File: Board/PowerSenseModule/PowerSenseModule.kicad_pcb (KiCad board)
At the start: 2 copper layers, 54 parts, among them J1 Power IO, J2 CAN IO, J3 Programming Header, U1 TPS82150, U2 ZLDO117, U3 dsPIC33EP32GP502_QFN, U4 MCP2542FDxMF, U5 MCP9700AT-ETT, U6 MCP39F511A

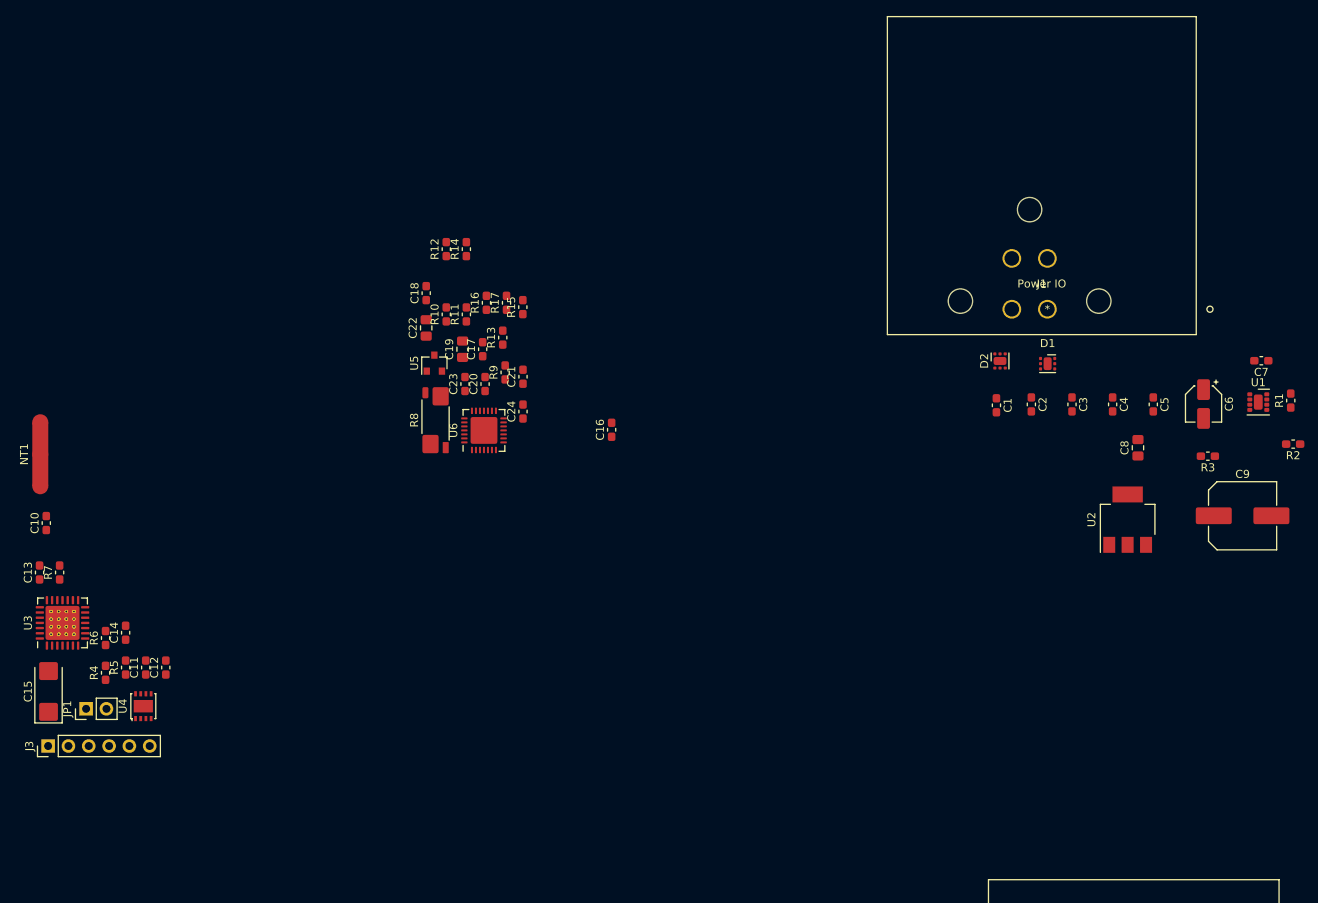
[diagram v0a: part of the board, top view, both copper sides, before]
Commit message: Moses's changes, removed MPLAB proj
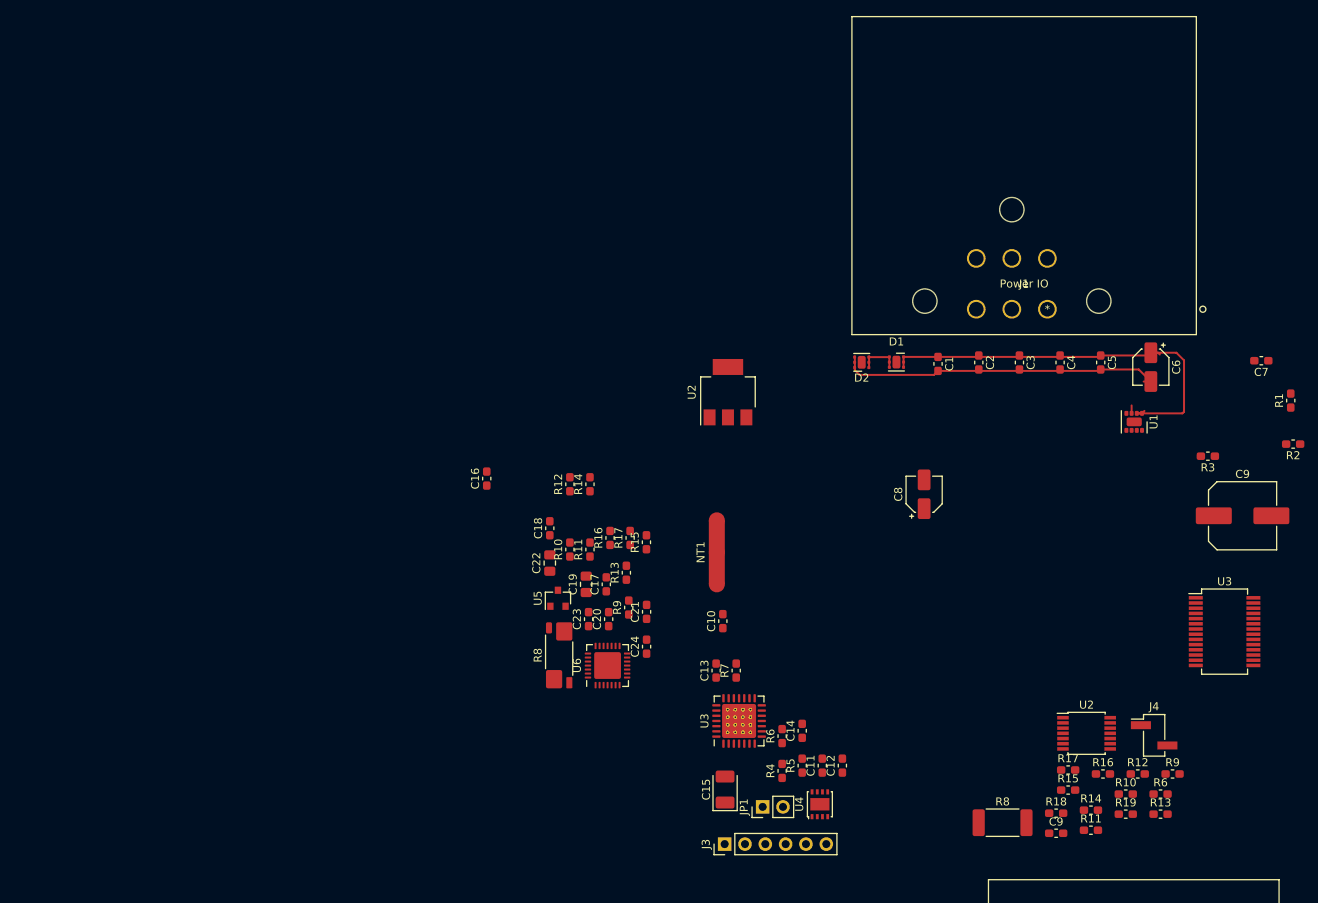
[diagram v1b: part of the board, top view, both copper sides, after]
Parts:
- added C9: 33nF, Capacitor_SMD:C_0603_1608Metric_Pad1.05x0.95mm_HandSolder, F.Cu at (156.0, 116.3)
- added J4: Conn_01x02_Male, Connector_PinHeader_2.54mm:PinHeader_1x02_P2.54mm_Vertical_SMD_Pin1Left, F.Cu at (168.3, 104.1)
- added R10: 12k, Capacitor_SMD:C_0603_1608Metric_Pad1.05x0.95mm_HandSolder, F.Cu at (164.7, 111.4)
- added R11: 12k, Capacitor_SMD:C_0603_1608Metric_Pad1.05x0.95mm_HandSolder, F.Cu at (160.4, 115.9)
- added R12: 180k, Capacitor_SMD:C_0603_1608Metric_Pad1.05x0.95mm_HandSolder, F.Cu at (166.2, 108.9)
- added R13: 180k, Capacitor_SMD:C_0603_1608Metric_Pad1.05x0.95mm_HandSolder, F.Cu at (169.1, 113.9)
- added R14: 1k, Capacitor_SMD:C_0603_1608Metric_Pad1.05x0.95mm_HandSolder, F.Cu at (160.4, 113.4)
- added R15: 10k, Capacitor_SMD:C_0603_1608Metric_Pad1.05x0.95mm_HandSolder, F.Cu at (157.5, 110.9)
- added R16: 10k, Capacitor_SMD:C_0603_1608Metric_Pad1.05x0.95mm_HandSolder, F.Cu at (161.9, 108.9)
- added R17: 499k, Resistor_SMD:R_0603_1608Metric_Pad1.05x0.95mm_HandSolder, F.Cu at (157.5, 108.4)
- added R18: 499k, Resistor_SMD:R_0603_1608Metric_Pad1.05x0.95mm_HandSolder, F.Cu at (156.0, 113.8)
- added R19: 499k, Resistor_SMD:R_0603_1608Metric_Pad1.05x0.95mm_HandSolder, F.Cu at (164.7, 113.9)
- added R6: 0, Capacitor_SMD:C_0603_1608Metric_Pad1.05x0.95mm_HandSolder, F.Cu at (169.1, 111.4)
- added R8: 4m, Resistor_SMD:R_2512_6332Metric_Pad1.52x3.35mm_HandSolder, F.Cu at (149.3, 115.0)
- added R9: 0, Capacitor_SMD:C_0603_1608Metric_Pad1.05x0.95mm_HandSolder, F.Cu at (170.6, 108.9)
- added U2: NCV2007x, Package_SO:TSSOP-14_4.4x5mm_P0.65mm, F.Cu at (159.8, 103.8)
- added U3: dsPIC33EV32GM102, Package_SO:SSOP-28_5.3x10.2mm_P0.65mm, F.Cu at (177.1, 91.1)
- C15: footprint Capacitor_Tantalum_SMD:CP_EIA-6032-28_Kemet-C_Pad2.25x2.35mm_HandSolder -> Capacitor_Tantalum_SMD:CP_EIA-3528-12_Kemet-T_Pad1.50x2.35mm_HandSolder
- C6: value 10uF -> 47uF
- C8: footprint Capacitor_SMD:C_0805_2012Metric_Pad1.15x1.40mm_HandSolder -> Capacitor_SMD:CP_Elec_4x5.8
- J1: footprint Connector_TE:DT13-4P -> Connector_TE:DT13-6P
- moved C10 85.5 mm to (114.4, 89.8)
- moved C14 85.5 mm to (124.3, 103.5)
- moved C15 85.5 mm to (114.7, 110.8)
- moved NT1 85.5 mm to (113.6, 81.2)
- moved R5 85.5 mm to (124.3, 107.8)
- moved R7 85.5 mm to (116.0, 96.0)
- moved U3 85.5 mm to (116.4, 102.3)
- moved C11 85.5 mm to (126.8, 107.8)
- moved C12 85.5 mm to (129.3, 107.8)
- moved C13 85.5 mm to (113.5, 96.0)
- moved J3 85.5 mm to (114.6, 117.7)
- moved JP1 85.5 mm to (119.3, 113.0)
- moved R4 85.5 mm to (121.8, 108.5)
- moved R6 85.5 mm to (121.8, 104.2)
- moved U4 85.5 mm to (126.5, 112.7)
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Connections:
- C1 pad 1: /Power Sensing/Live_IN -> +12V
- C10 pad 1: +3V3 -> +5V
- C11 pad 1: +3V3 -> +5V
- C2 pad 1: /Power Sensing/Live_IN -> +12V
- C3 pad 1: /Power Sensing/Live_IN -> +12V
- C4 pad 1: /Power Sensing/Live_IN -> +12V
- C5 pad 1: /Power Sensing/Live_IN -> +12V
- C6 pad 1: /Power Sensing/Live_IN -> +12V
- D1 pad 1: /Power Sensing/Live_IN -> +12V
- J1 pad 1: /Power Sensing/Live_IN -> +12V
- J1 pad 3: /Power Sensing/Live_OUT -> /MCU and CAN/MEASURE_OUT
- J3 pad 2: +3V3 -> +5V
- R4 pad 1: +3V3 -> +5V
- U1 pad 1: /Power Sensing/Live_IN -> +12V
- U1 pad 2: /Power Sensing/Live_IN -> +12V
- U4 pad 1: Net-(U3-Pad19) -> Net-(U4-Pad1)
- U4 pad 4: Net-(U3-Pad20) -> Net-(U3-Pad23)
- U4 pad 5: +3V3 -> +5V
- U4 pad 8: Net-(U3-Pad21) -> Net-(U3-Pad24)
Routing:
- net +12V: track 0.00 -> 51.7 mm
- net GND: track 0.00 -> 41.7 mm
- net Net-(D1-Pad2): track 0.00 -> 5.18 mm

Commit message: BASE/REFERENCE
Initial Design.
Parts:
- removed C16, C17: 3.3nF, Capacitor_SMD:C_0603_1608Metric_Pad1.05x0.95mm_HandSolder
- removed C18: 820pF, Capacitor_SMD:C_0603_1608Metric_Pad1.05x0.95mm_HandSolder
- removed C19, C22: 1uF, Capacitor_SMD:C_0805_2012Metric_Pad1.15x1.40mm_HandSolder
- removed C20, C23, C24: 0.1uF, Capacitor_SMD:C_0603_1608Metric_Pad1.05x0.95mm_HandSolder
- removed C21: 0.01uF, Capacitor_SMD:C_0603_1608Metric_Pad1.05x0.95mm_HandSolder
- removed the C9 at (179.3, 76.6)
- removed J2: CAN IO, Connector_TE:DT13-2P
- removed the R10 at (95.2, 80.8)
- removed the R11 at (97.8, 80.8)
- removed the R12 at (95.2, 72.7)
- removed the R13 at (102.3, 83.7)
- removed the R14 at (97.8, 72.7)
- removed the R15 at (104.8, 79.9)
- removed the R16 at (100.3, 79.4)
- removed the R17 at (102.8, 79.4)
- removed the R6 at (121.8, 104.2)
- removed the R8 at (93.9, 94.1)
- removed the R9 at (102.6, 88.1)
- removed the U2 at (115.0, 61.2)
- removed the U3 at (116.4, 102.3)
- removed U5: MCP9700AT-ETT, Package_TO_SOT_SMD:SOT-23
- removed U6: MCP39F511A, Package_DFN_QFN:QFN-28-1EP_5x5mm_P0.5mm_EP3.35x3.35mm
- added D3: LED, Resistor_SMD:R_0603_1608Metric_Pad1.05x0.95mm_HandSolder, F.Cu at (29.2, 141.3)
- added D4: LED, Resistor_SMD:R_0603_1608Metric_Pad1.05x0.95mm_HandSolder, F.Cu at (29.2, 143.8)
- added R20: 300, Resistor_SMD:R_0603_1608Metric_Pad1.05x0.95mm_HandSolder, F.Cu at (33.5, 141.3)
- added R21: 300, Resistor_SMD:R_0603_1608Metric_Pad1.05x0.95mm_HandSolder, F.Cu at (33.5, 143.8)
- J1: value Power IO -> Conn_01x06_Male
- moved J1 130.5 mm to (52.1, 131.1)
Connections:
- J1 pad 5: (no net) -> /MCU and CAN/CANH
- J1 pad 6: (no net) -> /MCU and CAN/CANL
- U3 pad 11: Net-(U3-Pad11) -> GNDD
- U3 pad 12: Net-(U3-Pad12) -> GNDD
- U3 pad 14: Net-(U3-Pad14) -> GNDD
- U3 pad 15: Net-(U3-Pad15) -> GNDD
- U3 pad 17: Net-(U3-Pad17) -> GNDD
- U3 pad 18: Net-(U3-Pad18) -> Net-(U2-Pad13)
- U3 pad 2: Net-(R15-Pad2) -> Net-(C12-Pad1)
- U3 pad 21: Net-(U3-Pad21) -> GNDD
- U3 pad 25: Net-(U3-Pad25) -> GNDD
- U3 pad 26: Net-(U3-Pad26) -> GNDD
- U3 pad 3: Net-(U3-Pad3) -> Net-(R15-Pad2)
- U3 pad 6: Net-(U3-Pad6) -> GNDD
- U3 pad 7: Net-(U2-Pad13) -> GNDD
- U4 pad 1: Net-(U4-Pad1) -> Net-(U3-Pad22)

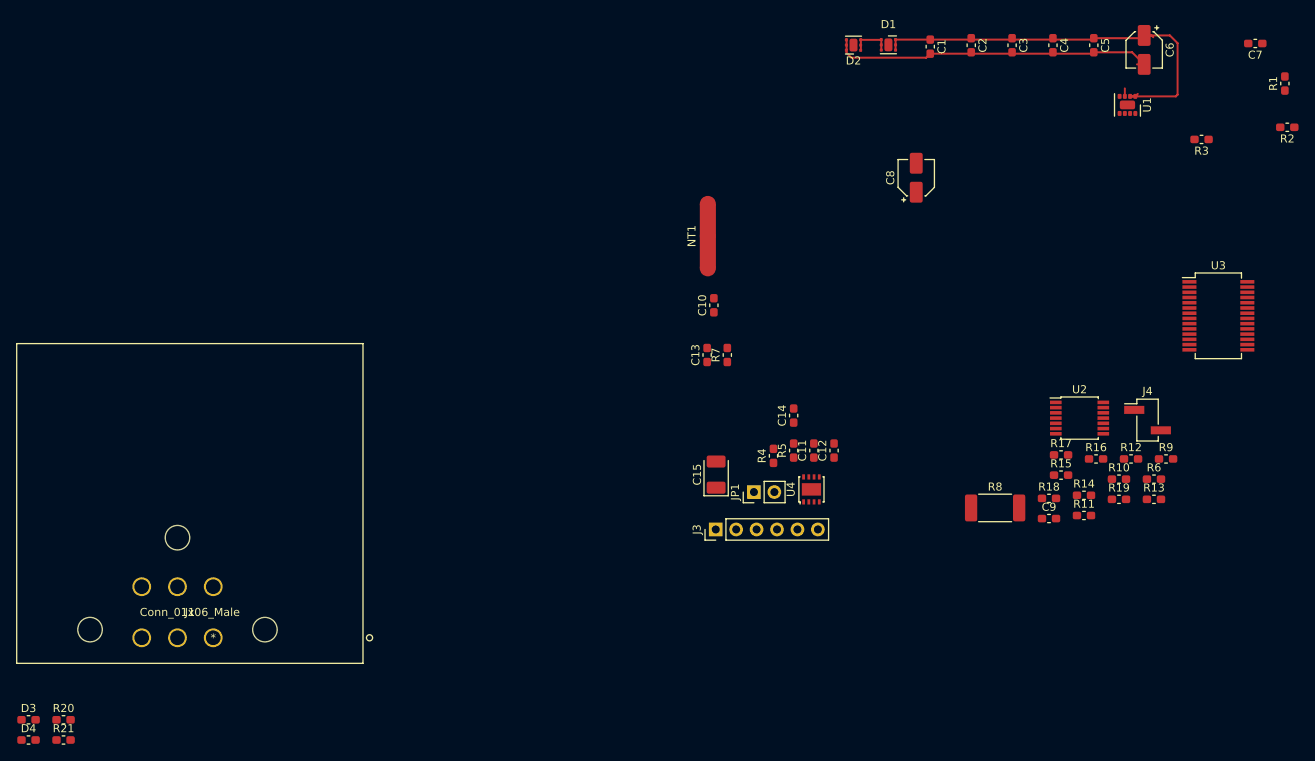
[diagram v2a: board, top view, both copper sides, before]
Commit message: FINAL BASIS/REFERENCE
Rewiring done to proper pins on MCU
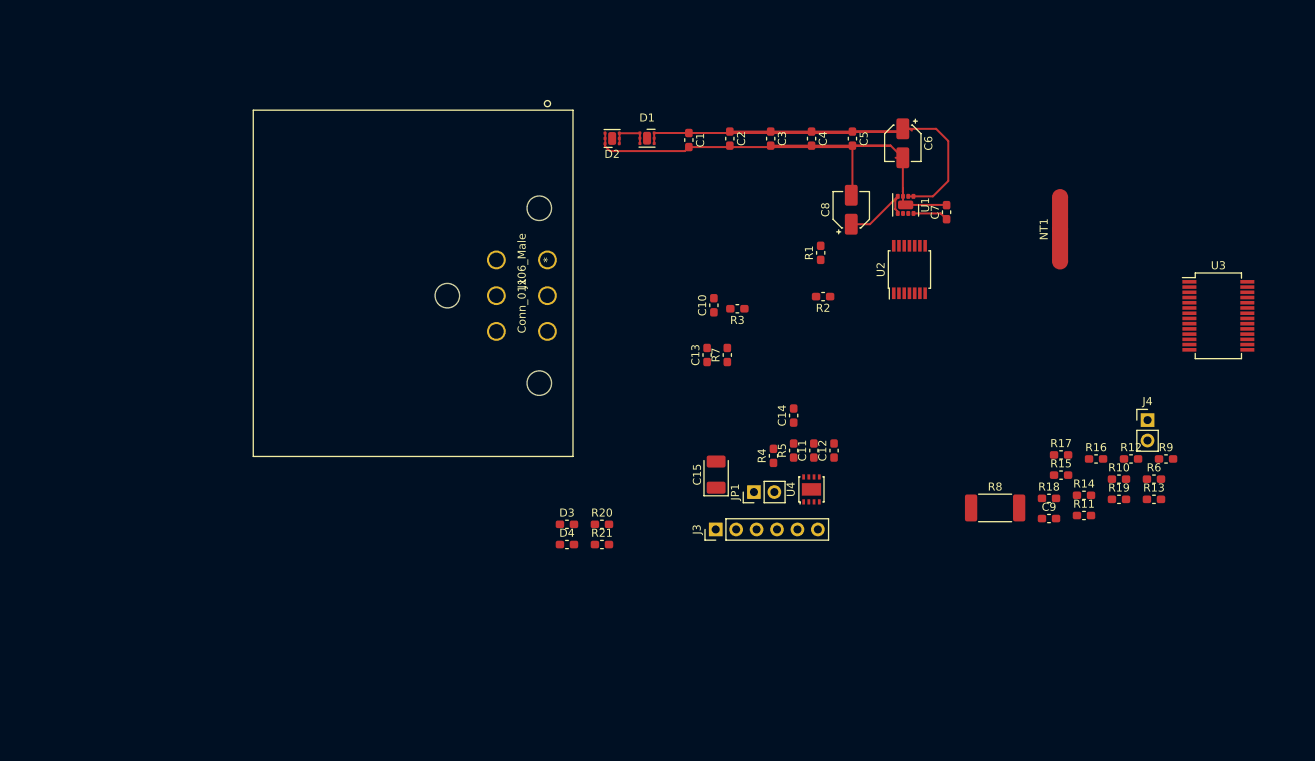
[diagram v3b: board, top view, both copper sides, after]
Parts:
- J4: footprint Connector_PinHeader_2.54mm:PinHeader_1x02_P2.54mm_Vertical_SMD_Pin1Left -> Connector_PinHeader_2.54mm:PinHeader_1x02_P2.54mm_Vertical
- moved D4 71.2 mm to (96.1, 119.5)
- moved R21 71.2 mm to (100.5, 119.5)
- moved D3 71.2 mm to (96.1, 117.0)
- moved R20 71.2 mm to (100.5, 117.0)
- moved J1 62.7 mm to (93.7, 84.2), turned to 90 degrees
- moved R1 61.4 mm to (127.7, 83.3)
- moved R2 61.4 mm to (128.0, 88.7)
- moved R3 61.4 mm to (117.3, 90.2)
- moved NT1 43.8 mm to (157.4, 80.3)
- moved C7 43.7 mm to (143.3, 78.2), turned to 90 degrees
- moved C1 32.2 mm to (111.3, 69.2)
- moved C2 32.2 mm to (116.4, 69.1)
- moved C4 32.2 mm to (126.5, 69.1)
- moved C3 32.2 mm to (121.4, 69.1)
- moved C5 32.2 mm to (131.6, 69.1)
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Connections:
- U3 pad 10: Net-(R21-Pad2) -> GNDD
- U3 pad 16: Net-(R18-Pad1) -> GNDD
- U3 pad 18: Net-(U2-Pad13) -> GNDD
- U3 pad 25: GNDD -> Net-(R20-Pad2)
- U3 pad 26: GNDD -> Net-(R21-Pad2)
- U3 pad 3: Net-(R15-Pad2) -> Net-(U3-Pad3)
- U3 pad 4: Net-(J3-Pad4) -> Net-(U2-Pad13)
- U3 pad 5: Net-(J3-Pad5) -> Net-(R18-Pad1)
- U3 pad 6: GNDD -> Net-(J3-Pad5)
- U3 pad 7: GNDD -> Net-(J3-Pad4)
- U3 pad 9: Net-(R20-Pad2) -> GNDD
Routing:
- net GND: track 41.7 -> 73.4 mm
- net +12V: track 51.7 -> 71.8 mm
- net +5V: track 0.00 -> 9.66 mm
- net Net-(C7-Pad1): track 0.00 -> 4.41 mm

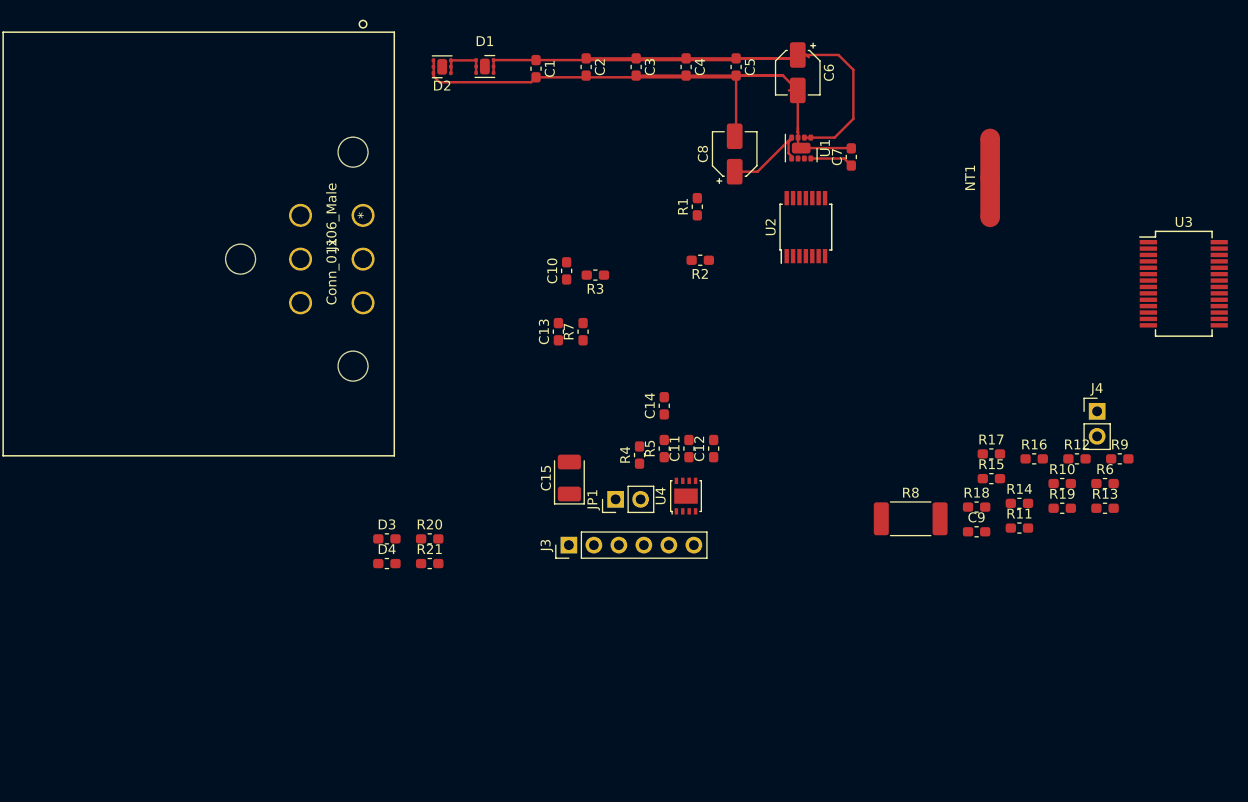
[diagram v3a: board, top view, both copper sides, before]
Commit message: PCB - Power tracing
Front tracing for most part done.
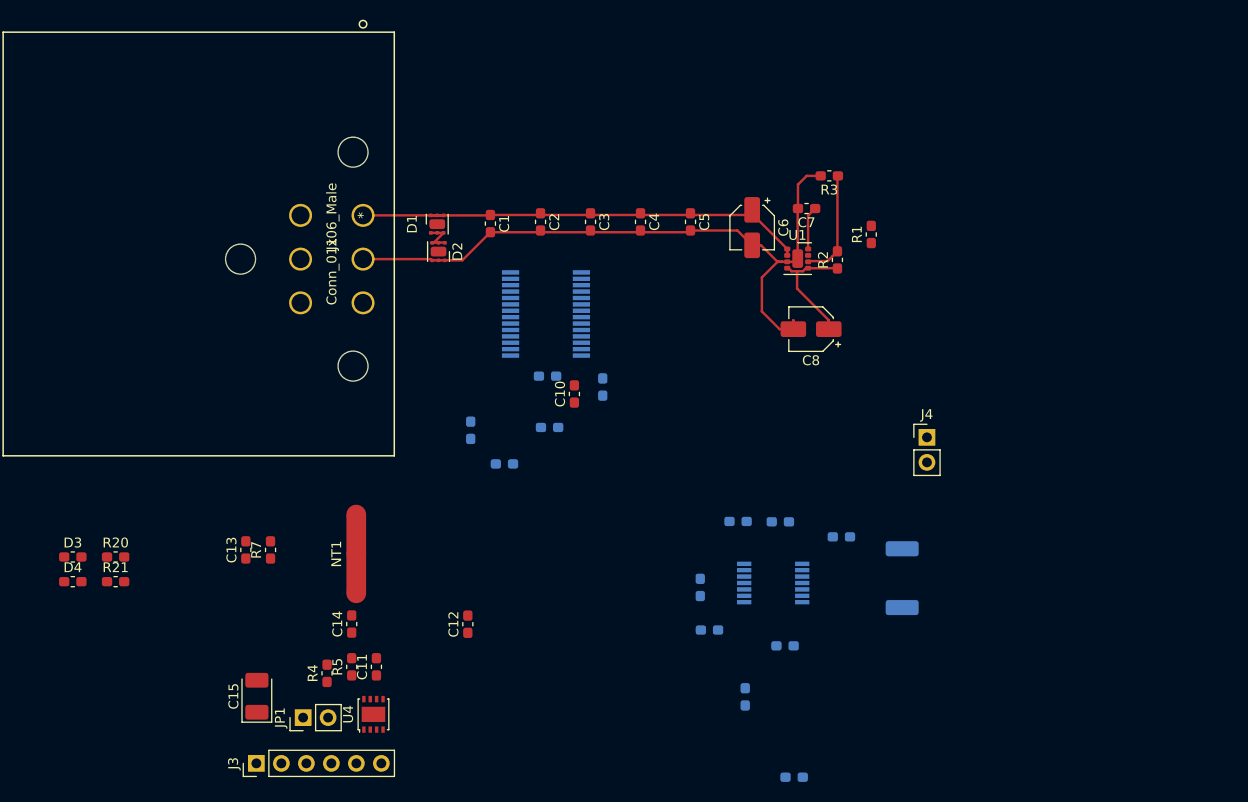
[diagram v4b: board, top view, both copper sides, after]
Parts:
- C9, R10, R11, R12, R13, R14, R15, R16, R17, R18, R19, R6, R8, R9, U2, U3: moved to B.Cu
- moved NT1 74.9 mm to (93.0, 118.6)
- moved U3 64.9 mm to (112.3, 94.2)
- moved R16 57.3 mm to (104.6, 106.0), turned to 90 degrees
- moved R19 54.0 mm to (112.4, 100.5), turned to 180 degrees
- moved R15 49.5 mm to (108.0, 109.4)
- moved R9 46.3 mm to (137.5, 141.2), turned to 180 degrees
- moved R18 44.1 mm to (112.6, 105.7), turned to 180 degrees
- moved R12 40.5 mm to (128.0, 122.0), turned to 90 degrees
- moved R17 40.1 mm to (118.0, 101.6), turned to 90 degrees
- moved C13 38.7 mm to (81.8, 118.2)
- moved C14 38.7 mm to (92.5, 125.7)
- moved C15 38.7 mm to (82.9, 133.0)
- moved R5 38.7 mm to (92.5, 130.0)
- moved R7 38.7 mm to (84.3, 118.2)
- moved U4 38.7 mm to (94.7, 134.9)
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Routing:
- net +12V: track 71.8 -> 46.8 mm
- net Net-(R2-Pad2): track 0.00 -> 11.1 mm
- net GND: track 73.4 -> 68.1 mm
- net +5V: track 9.66 -> 12.6 mm
- net Net-(D1-Pad2): track 5.18 -> 4.16 mm
